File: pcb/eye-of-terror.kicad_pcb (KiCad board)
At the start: 4 copper layers, 200 x 200 mm, 226 parts, among them J1 Conn_01x02_Socket, J2 G-Switch GT-USB-7055E, J3 Conn_01x04, J4 Conn_01x04, J5 Conn_01x03, J6 Conn_01x02_Socket, J7 Conn_01x02_Socket, J8 Conn_01x03, Q1 IPT020N10N3, Q10 ALS-PT19-315C/L177/TR8, Q11 ALS-PT19-315C/L177/TR8, Q12 ALS-PT19-315C/L177/TR8, Q13 ALS-PT19-315C/L177/TR8, Q14 ALS-PT19-315C/L177/TR8, Q15 ALS-PT19-315C/L177/TR8, Q16 ALS-PT19-315C/L177/TR8, Q2 IPT020N10N3, Q3 IPT020N10N3, Q4 IPT020N10N3, Q5 IPT020N10N3, Q6 IPT020N10N3, Q7 ALS-PT19-315C/L177/TR8, Q8 ALS-PT19-315C/L177/TR8, Q9 ALS-PT19-315C/L177/TR8, SW1 SW_Push, SW2 SW_Push, U1 RP2350B, U2 TD1660, U3 AP63205WU-7, U4 LSM6DS3, U5 W25Q32JVSS, U7 DRV8353HRTAR, Y1 ABM8-272-T3

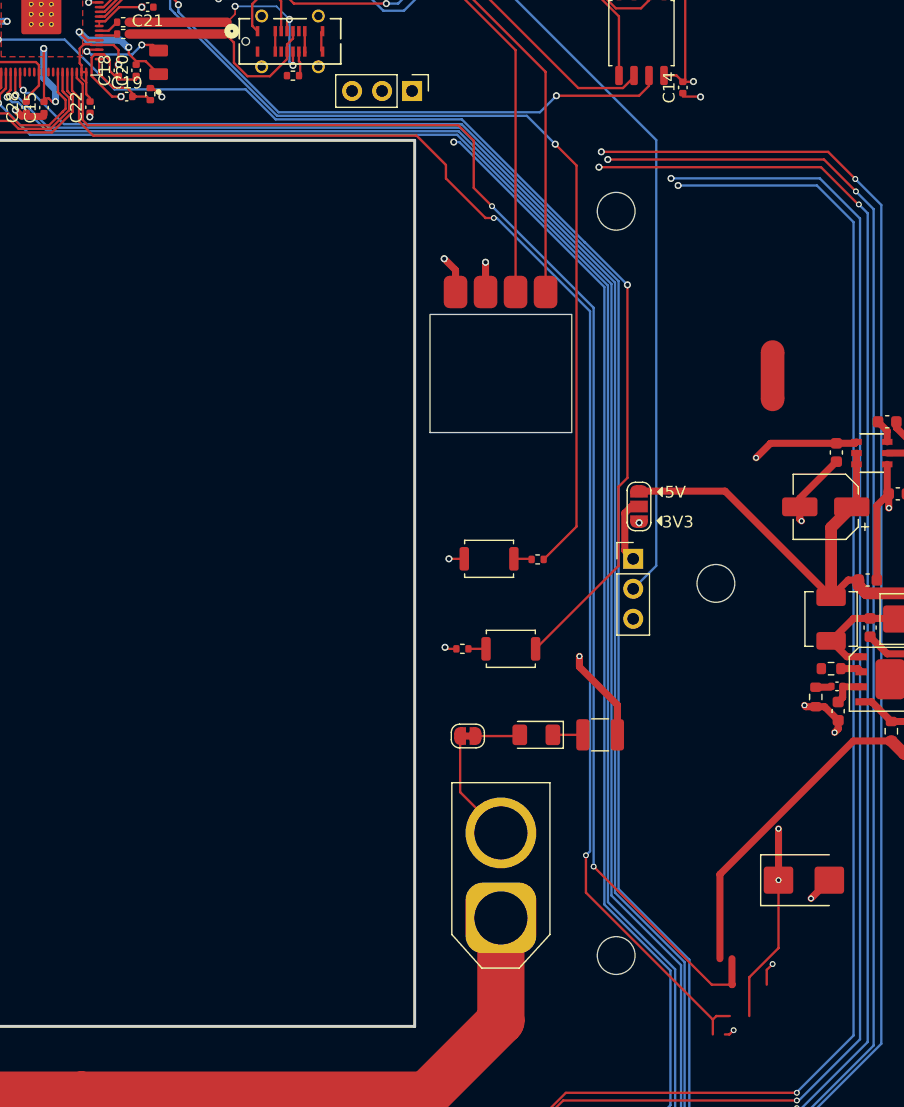
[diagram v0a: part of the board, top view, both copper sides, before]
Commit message: BOM fully updated, added diodes
* added another Schottky diode for USB backfeed from 5V line
* added ESD protection to USB data lines
* for some reason, LCSC numbers disappeared (i forgot if they were ever
  there), so LCSC numbers added
* BOM in schematic matches BOM in Notion
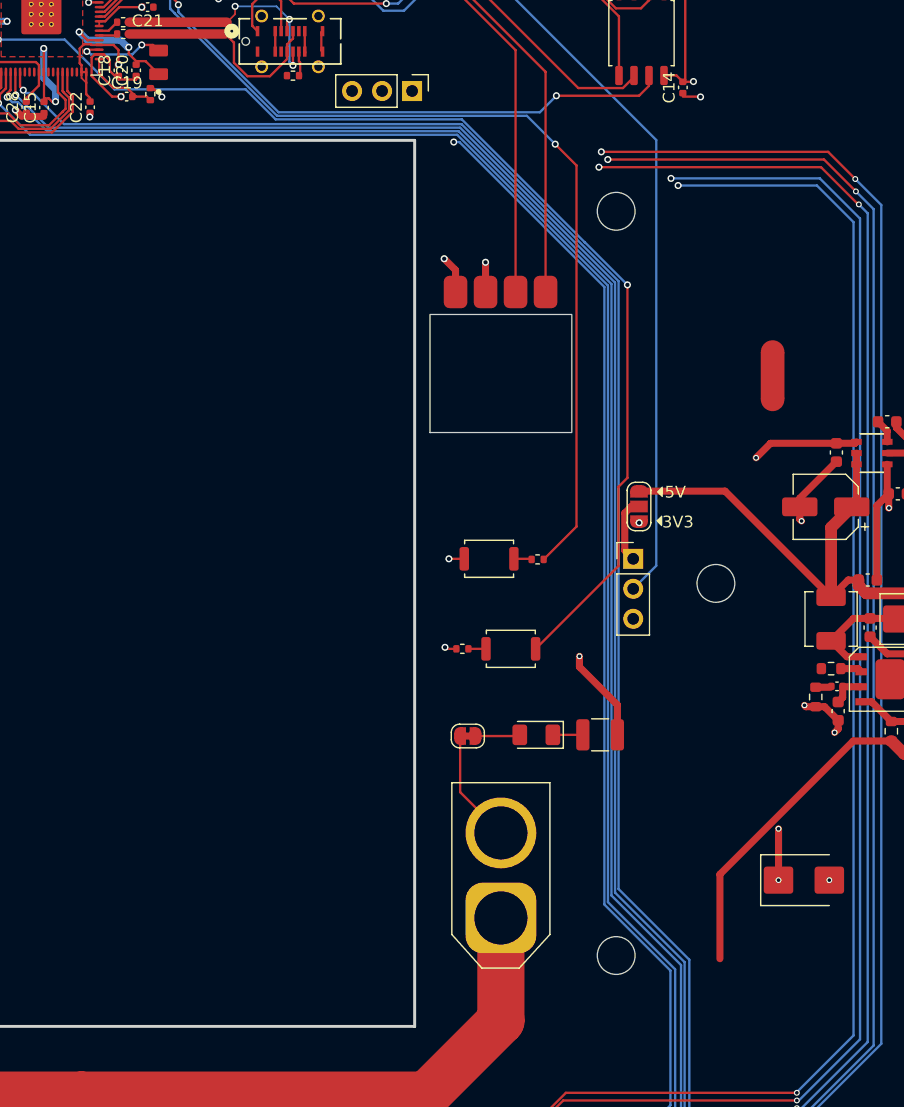
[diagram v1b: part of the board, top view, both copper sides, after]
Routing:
- net /BATT_MON: track 122.4 -> 0.00 mm, vias 2 -> 0
- net /5V_MON: track 121.8 -> 0.00 mm, vias 2 -> 0
- net +BATT: track 235.5 -> 223.0 mm
- net DGND: track 105.4 -> 102.5 mm, vias 33 -> 31
- net PGND: track 268.8 -> 266.6 mm

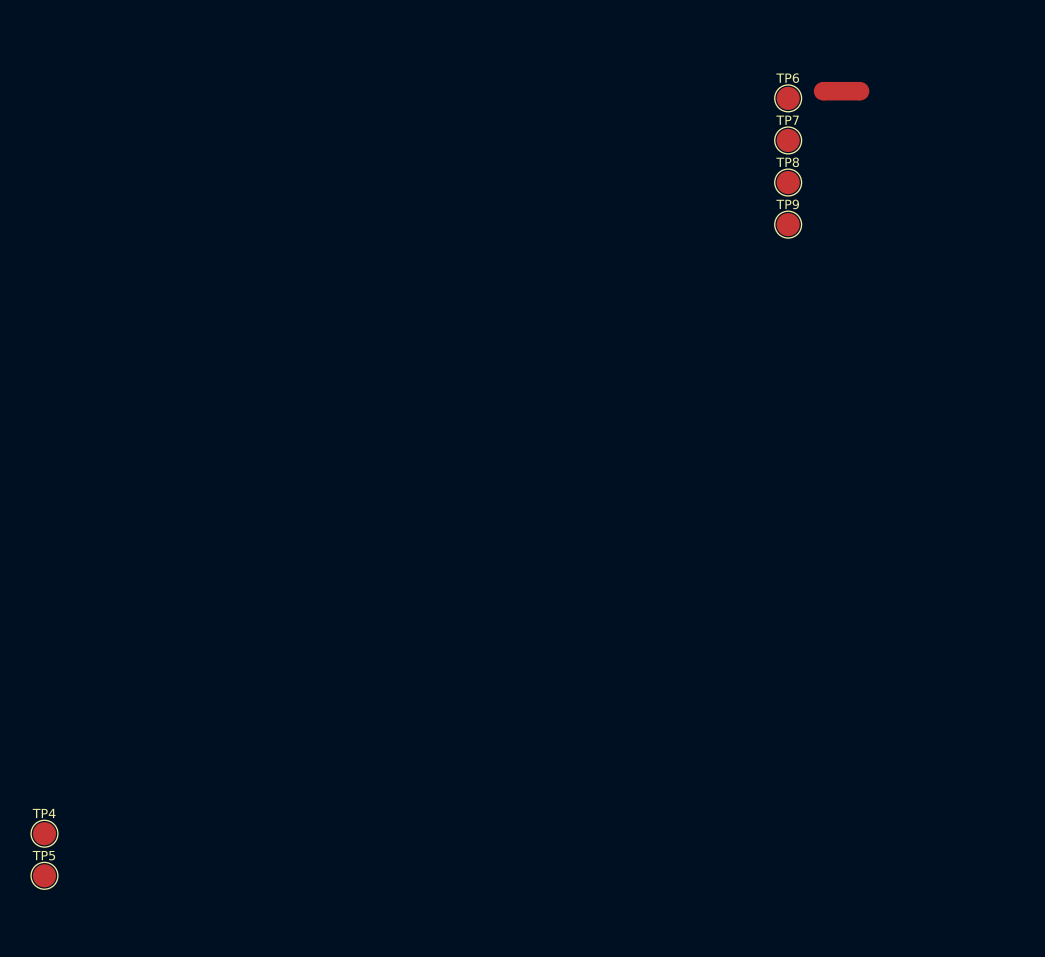
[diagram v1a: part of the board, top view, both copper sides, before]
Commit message: added footprints for motor winding connections
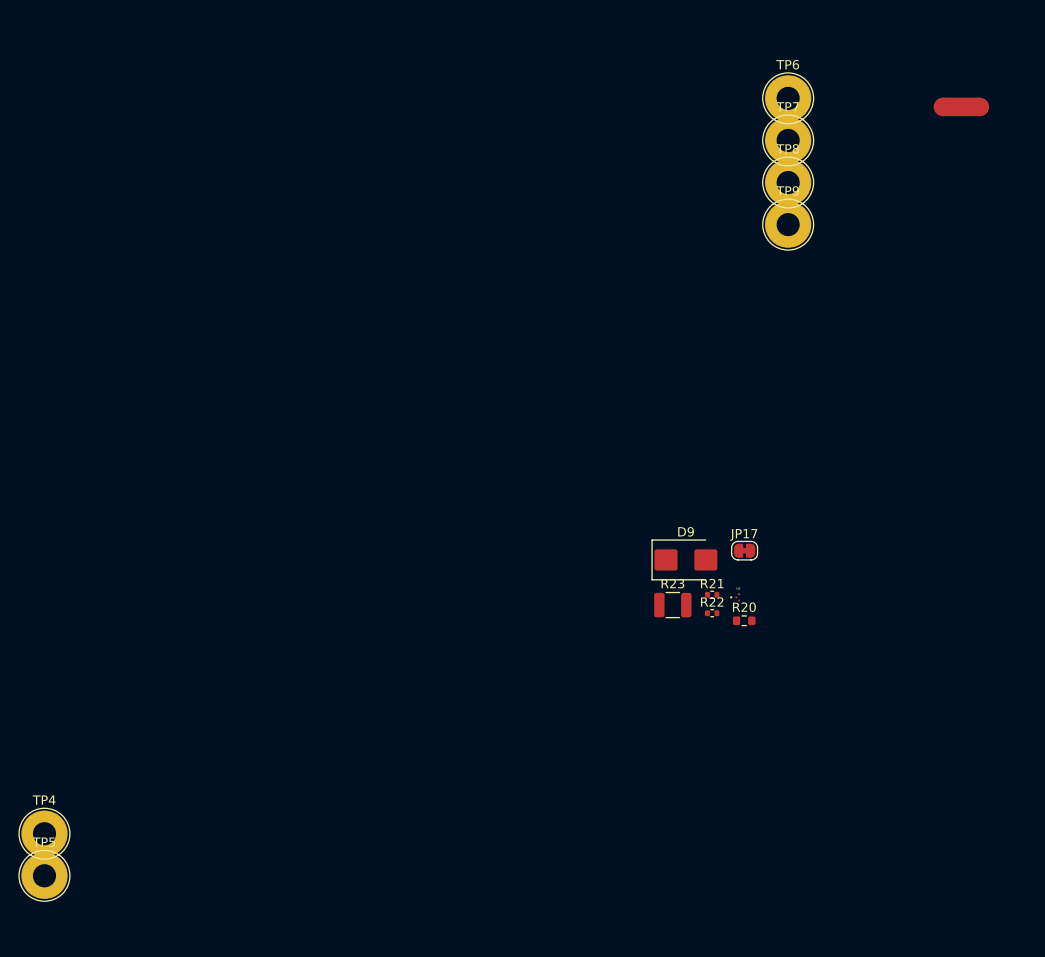
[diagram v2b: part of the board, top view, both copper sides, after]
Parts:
- added D9: SS36, Diode_SMD:D_SMB, F.Cu at (159.3, 197.5)
- added JP17: SolderJumper_2_Bridged, Jumper:SolderJumper-2_P1.3mm_Bridged_RoundedPad1.0x1.5mm, F.Cu at (165.7, 196.5)
- added R20: 68k, Resistor_SMD:R_0603_1608Metric, F.Cu at (165.6, 204.1)
- added R21: 10k, Resistor_SMD:R_0402_1005Metric, F.Cu at (162.2, 201.2)
- added R22: 1k, Resistor_SMD:R_0402_1005Metric, F.Cu at (162.2, 203.2)
- added R23: 1.5k, Resistor_SMD:R_1210_3225Metric, F.Cu at (157.9, 202.4)
- added U8: ESD122DMXR, ESD122DMXR:IC_ESD122DMXR, F.Cu at (164.9, 201.5)
- TP4, TP5, TP6, TP7, TP8, TP9: footprint TestPoint:TestPoint_Pad_D2.5mm -> motor-phase-connection:THTPad_D5.0mm_Drill2.5mm
- moved NT2 13.1 mm to (189.1, 148.5)
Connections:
- net VBUS renamed Net-(D9-A)

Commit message: WIP time to do layout again
* moved some more stuff to the back of the board
* need to move more stuff
* deleted all traces and vias
* changed standard SMD footprints to hand-solder version
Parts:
- added JP18: SolderJumper_2_Bridged, Jumper:SolderJumper-2_P1.3mm_Bridged_RoundedPad1.0x1.5mm, F.Cu at (465.8, 188.1)
- added Q17: NMOS, Package_TO_SOT_SMD:TSOT-23_HandSoldering, F.Cu at (466.3, 184.1)
- added R24: 10k, Resistor_SMD:R_0402_1005Metric_Pad0.72x0.64mm_HandSolder, F.Cu at (469.4, 187.4)
- C10, C11, C12, C13, C14, C15, C16, C17, C18, C19, C20, C21, C22, C23, C24, C25, C26, C27, C28, C29, C5, C8: footprint Capacitor_SMD:C_0402_1005Metric -> Capacitor_SMD:C_0402_1005Metric_Pad0.74x0.62mm_HandSolder
- C2, C3, C35, C36, C37, C38, C4, C6, C7, C9: footprint Capacitor_SMD:C_0603_1608Metric -> Capacitor_SMD:C_0603_1608Metric_Pad1.08x0.95mm_HandSolder
- C30, C31, C33, C34: footprint Capacitor_SMD:C_0603_1608Metric -> Capacitor_SMD:C_0603_1608Metric_Pad1.08x0.95mm_HandSolder; moved to B.Cu
- C32: footprint Capacitor_SMD:C_0402_1005Metric -> Capacitor_SMD:C_0402_1005Metric_Pad0.74x0.62mm_HandSolder; moved to B.Cu
- D13, D16, D18, D19, D20, D21, D22, D23, D3, D4, D5, D6, D7, D8: footprint Diode_SMD:D_1206_3216Metric -> Diode_SMD:D_1206_3216Metric_Pad1.42x1.75mm_HandSolder
- Q10, Q11, Q7, Q8, Q9: footprint LED_SMD:LED_0603_1608Metric -> LED_SMD:LED_0603_1608Metric_Pad1.05x0.95mm_HandSolder
- R1, R10, R11, R12, R13, R14, R15, R16, R2, R21, R22, R4, R43, R44, R45, R46, R47, R48, R49, R50, R51, R55, R8, R9: footprint Resistor_SMD:R_0402_1005Metric -> Resistor_SMD:R_0402_1005Metric_Pad0.72x0.64mm_HandSolder
- R17, R18, R19: footprint Resistor_SMD:R_1206_3216Metric -> Resistor_SMD:R_1206_3216Metric_Pad1.30x1.75mm_HandSolder
- R20, R25, R26, R27, R28, R29, R3, R30, R35, R38, R5, R6, R7: footprint Resistor_SMD:R_0603_1608Metric -> Resistor_SMD:R_0603_1608Metric_Pad0.98x0.95mm_HandSolder
- R23: footprint Resistor_SMD:R_1210_3225Metric -> Resistor_SMD:R_1210_3225Metric_Pad1.30x2.65mm_HandSolder
- R40: footprint Resistor_SMD:R_1210_3225Metric -> Resistor_SMD:R_0603_1608Metric_Pad0.98x0.95mm_HandSolder
- moved Y1 163.7 mm to (463.8, 147.4), turned to 0 degrees
- moved R8 159.7 mm to (462.2, 154.8)
- moved C26 153.8 mm to (459.7, 142.9)
- moved C27 151.5 mm to (459.7, 144.9)
- moved C25 150.8 mm to (456.9, 148.8)
- moved C13 150.4 mm to (451.1, 142.9), turned to 0 degrees
- moved C28 146.9 mm to (459.7, 146.8), turned to 0 degrees
- moved C16 145.2 mm to (451.1, 146.8)
- moved C23 144.8 mm to (456.9, 144.9), turned to 0 degrees
- moved L3 140.4 mm to (464.4, 143.5), turned to 0 degrees
- moved C22 139.1 mm to (456.9, 142.9), turned to 0 degrees
- moved C24 138.8 mm to (456.9, 146.8), turned to 0 degrees
- moved R12 138.4 mm to (462.2, 156.7), turned to 0 degrees
- moved C15 137.0 mm to (451.1, 144.9), turned to 0 degrees
- moved C17 136.9 mm to (451.1, 148.8), turned to 0 degrees
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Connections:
- R44 pad 2: DGND -> /ENC_LED_OUT
- R45 pad 2: DGND -> /ENC_LED_OUT
- R47 pad 2: DGND -> /ENC_LED_OUT
- R49 pad 2: DGND -> /ENC_LED_OUT
- R51 pad 2: DGND -> /ENC_LED_OUT
- R52 pad 2: DGND -> /ENC_LED_OUT
- R53 pad 2: DGND -> /ENC_LED_OUT
- R54 pad 2: DGND -> /ENC_LED_OUT
- R59 pad 2: DGND -> /ENC_LED_OUT
- R60 pad 2: DGND -> /ENC_LED_OUT
- U1 pad 47: unconnected-(U1-GPIO38-Pad47) -> /ENC_LED_DRV
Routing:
- net PGND: track 266.6 -> 0.00 mm, vias 23 -> 0
- net /ENC_SENSE_1: track 255.5 -> 0.00 mm, vias 4 -> 0
- net /ENC_SENSE_2: track 252.0 -> 0.00 mm, vias 4 -> 0
- net /ENC_SENSE_3: track 249.1 -> 0.00 mm, vias 4 -> 0
- net /ENC_SENSE_5: track 243.4 -> 0.00 mm, vias 3 -> 0
- net /ENC_SENSE_4: track 242.4 -> 0.00 mm, vias 3 -> 0
- net +BATT: track 223.0 -> 0.00 mm, vias 10 -> 0
- net /ENC_SENSE_10: track 209.1 -> 0.00 mm, vias 1 -> 0
- net /ENC_SENSE_9: track 207.9 -> 0.00 mm, vias 1 -> 0
- net /ENC_SENSE_8: track 206.8 -> 0.00 mm, vias 1 -> 0
- net /ENC_SENSE_6: track 205.0 -> 0.00 mm, vias 2 -> 0
- net /ENC_SENSE_7: track 205.0 -> 0.00 mm, vias 1 -> 0
- net +3V3: track 141.0 -> 0.00 mm, vias 33 -> 0
- net /GREEN_LED_1: track 138.1 -> 0.00 mm, vias 3 -> 0
- net /BLUE_LED_1: track 134.9 -> 0.00 mm, vias 3 -> 0
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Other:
- board text added: "5 4 3 2 1"
- board text removed: "4 5 3 2 1"

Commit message: WIP layout
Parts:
- added JP19: SolderJumper_2_Bridged, Jumper:SolderJumper-2_P1.3mm_Bridged_RoundedPad1.0x1.5mm, F.Cu at (360.4, 137.4)
- added JP20: SolderJumper_2_Bridged, Jumper:SolderJumper-2_P1.3mm_Bridged_RoundedPad1.0x1.5mm, F.Cu at (360.4, 148.2)
- added JP21: SolderJumper_2_Bridged, Jumper:SolderJumper-2_P1.3mm_Bridged_RoundedPad1.0x1.5mm, F.Cu at (360.4, 145.5)
- added JP22: SolderJumper_2_Bridged, Jumper:SolderJumper-2_P1.3mm_Bridged_RoundedPad1.0x1.5mm, F.Cu at (360.4, 140.1)
- added JP23: SolderJumper_2_Bridged, Jumper:SolderJumper-2_P1.3mm_Bridged_RoundedPad1.0x1.5mm, F.Cu at (360.4, 142.8)
- added JP24: SolderJumper_2_Bridged, Jumper:SolderJumper-2_P1.3mm_Bridged_RoundedPad1.0x1.5mm, F.Cu at (360.4, 150.9)
- C15, C16, C17, C18, C19, C20, C21, C22, C23, C24, C25, C26, C27, C28, C29, C35, D9, L3, R1, R12, R2, R20, R21, R22, R23, U6: moved to B.Cu
- D24, D25, D26, D27, D28: footprint Diode_SMD:D_1206_3216Metric -> Diode_SMD:D_1206_3216Metric_Pad1.42x1.75mm_HandSolder
- JP17: footprint Jumper:SolderJumper-2_P1.3mm_Bridged_RoundedPad1.0x1.5mm -> Jumper:SolderJumper-2_P1.3mm_Open_RoundedPad1.0x1.5mm; moved to B.Cu
- Q12, Q13, Q14, Q15, Q16: footprint LED_SMD:LED_0603_1608Metric -> LED_SMD:LED_0603_1608Metric_Pad1.05x0.95mm_HandSolder
- R52, R53, R54, R56, R57, R58, R59, R60, R63, R64: footprint Resistor_SMD:R_0402_1005Metric -> Resistor_SMD:R_0402_1005Metric_Pad0.72x0.64mm_HandSolder
- moved R23 267.8 mm to (423.4, 237.7)
- moved R22 261.8 mm to (422.1, 235.1), turned to 180 degrees
- moved R21 258.7 mm to (417.9, 240.4)
- moved R20 255.0 mm to (418.4, 237.6), turned to 180 degrees
- moved JP18 205.0 mm to (278.9, 272.6)
- moved Q17 205.0 mm to (279.5, 268.6)
- moved R24 205.0 mm to (282.6, 271.8)
- moved JP17 198.5 mm to (363.3, 215.1)
- moved D9 172.3 mm to (326.3, 154.9), turned to 135 degrees
- moved U8 168.5 mm to (325.9, 151.6), turned to 45 degrees
- moved Y1 159.4 mm to (304.8, 158.4), turned to -45 degrees
- moved R8 153.2 mm to (309.0, 158.2), turned to 135 degrees
- moved C27 153.0 mm to (307.0, 153.9), turned to 45 degrees
- moved C28 151.8 mm to (308.2, 155.2), turned to 45 degrees
- moved C24 151.1 mm to (305.8, 145.7), turned to -45 degrees
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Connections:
- R9 pad 2: /GPIO0 -> Net-(JP19-B)
- U5 pad 1: /GPIO0 -> Net-(JP19-B)
- U5 pad 2: /QSPI_SD1 -> Net-(JP22-B)
- U5 pad 3: /QSPI_SD2 -> Net-(JP23-B)
- U5 pad 5: /QSPI_SD0 -> Net-(JP21-B)
- U5 pad 6: /QSPI_SCLK -> Net-(JP20-B)
- U5 pad 7: /QSPI_SD3 -> Net-(JP24-B)
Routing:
- net +BATT: track 0.00 -> 300.0 mm, vias 0 -> 10
- net PGND: track 0.00 -> 279.3 mm, vias 0 -> 34
- net /ENC_SENSE_3: track 0.00 -> 151.1 mm, vias 0 -> 1
- net /ENC_SENSE_2: track 0.00 -> 150.6 mm, vias 0 -> 1
- net /ENC_SENSE_1: track 0.00 -> 149.6 mm, vias 0 -> 1
- net /ENC_SENSE_4: track 0.00 -> 147.4 mm, vias 0 -> 1
- net /ENC_LED_DRV: track 0.00 -> 146.7 mm, vias 0 -> 1
- net /ENC_SENSE_10: track 0.00 -> 146.5 mm, vias 0 -> 1
- net /ENC_SENSE_5: track 0.00 -> 145.4 mm, vias 0 -> 1
- net /ENC_SENSE_9: track 0.00 -> 145.3 mm, vias 0 -> 1
- net /ENC_SENSE_8: track 0.00 -> 145.0 mm, vias 0 -> 1
- net /ENC_SENSE_7: track 0.00 -> 144.7 mm, vias 0 -> 1
- net /ENC_SENSE_6: track 0.00 -> 144.0 mm, vias 0 -> 1
- net /QSPI_SS: track 0.00 -> 94.3 mm, vias 0 -> 2
- net /RUN: track 0.00 -> 92.2 mm, vias 0 -> 2
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- added copper zone on F.Cu, net +5V
- added copper zone on F.Cu, net +BATT
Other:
- board text added: "3V3 Reg."
- board text added: "5V Reg."
- board text added: "LED turns on when board is powered by battery. Cut this jumper to disable indicator LED."
- board text removed: "3V3"
- board text removed: "5V"

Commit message: WIP layout almost done
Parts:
- moved JP8 151.0 mm to (325.6, 119.2)
- moved J8 151.0 mm to (325.1, 123.7)
- moved R35 115.6 mm to (319.0, 119.3), turned to 90 degrees
- moved R38 113.5 mm to (315.7, 118.8), turned to 90 degrees
- moved D13 108.1 mm to (319.0, 123.6), turned to -90 degrees
- moved D16 104.9 mm to (315.7, 123.6), turned to -90 degrees
- moved R25 56.3 mm to (295.8, 69.4)
- moved D3 56.3 mm to (291.3, 69.4)
- moved D4 55.2 mm to (291.3, 73.6)
- moved R26 55.2 mm to (295.8, 73.6)
- moved D5 52.7 mm to (306.5, 70.1)
- moved R27 52.6 mm to (311.2, 70.1)
- moved D6 51.5 mm to (306.5, 74.3)
- moved R28 51.3 mm to (311.2, 74.3)
- moved R29 51.3 mm to (329.9, 70.1)
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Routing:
- net /IMU_CIPO: track 0.00 -> 94.4 mm, vias 0 -> 1
- net /IMU_COPI: track 0.00 -> 93.9 mm, vias 0 -> 1
- net /IMU_SCK: track 0.00 -> 93.8 mm, vias 0 -> 1
- net /IMU_CS: track 0.00 -> 93.3 mm, vias 0 -> 1
- net /SDA_TOP_IR_TOF: track 0.00 -> 82.6 mm, vias 0 -> 1
- net /SCL_TOP_IR_TOF: track 0.00 -> 80.6 mm, vias 0 -> 1
- net /SDA_BOT_IR_TOF: track 0.00 -> 66.6 mm, vias 0 -> 1
- net /SCL_BOT_IR_TOF: track 0.00 -> 65.4 mm, vias 0 -> 1
- net /SOC: track 3.02 -> 43.3 mm, vias 0 -> 2
- net /SOB: track 2.84 -> 41.6 mm, vias 0 -> 2
- net /SOA: track 2.67 -> 38.2 mm, vias 0 -> 2
- net /INLC: track 0.00 -> 29.7 mm
- net /INHC: track 0.00 -> 29.1 mm
- net /INLB: track 0.00 -> 27.4 mm
- net /INHB: track 0.00 -> 26.8 mm
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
